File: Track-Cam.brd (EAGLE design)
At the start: 65 x 56 mm, 37 parts, among them IC1 STM32F042KT/M, IC2 BD6211F/M, IC3 BD6211F/M, X1 RASPI_BOARD_B+#_HC

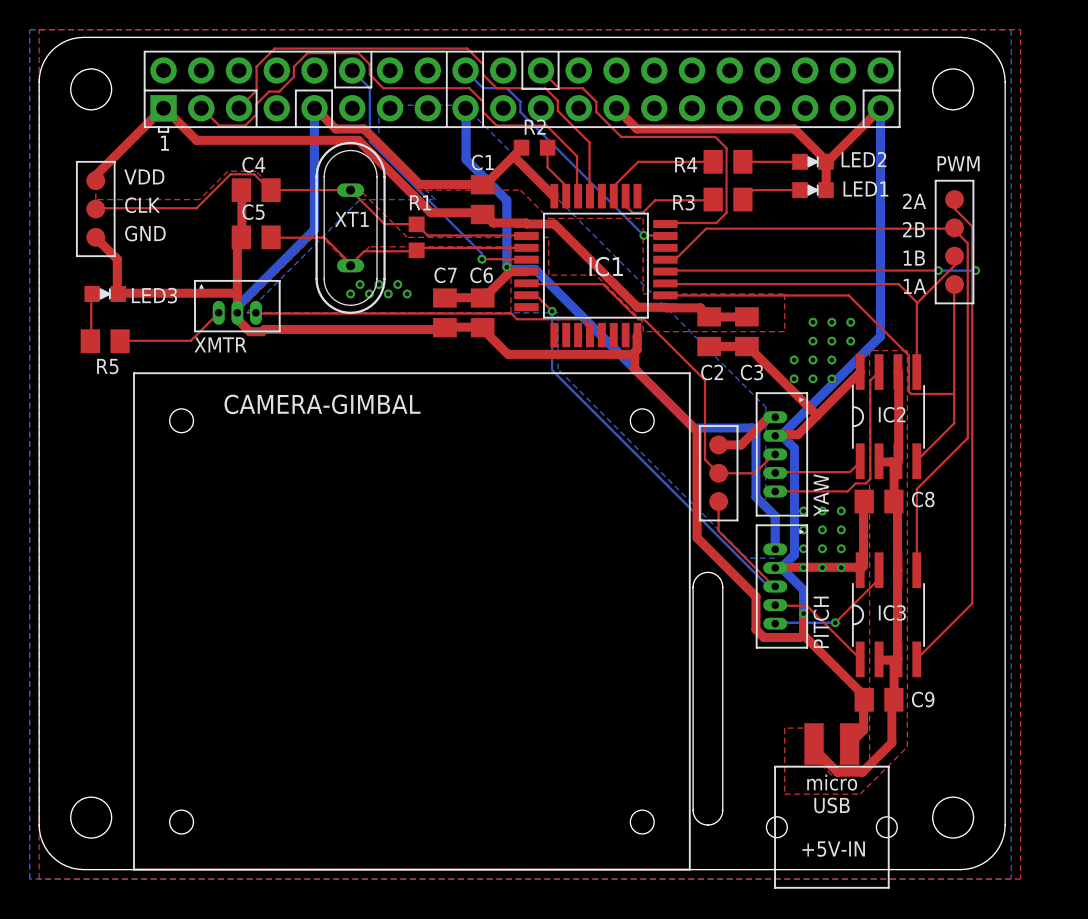
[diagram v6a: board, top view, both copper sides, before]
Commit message: improve silk design
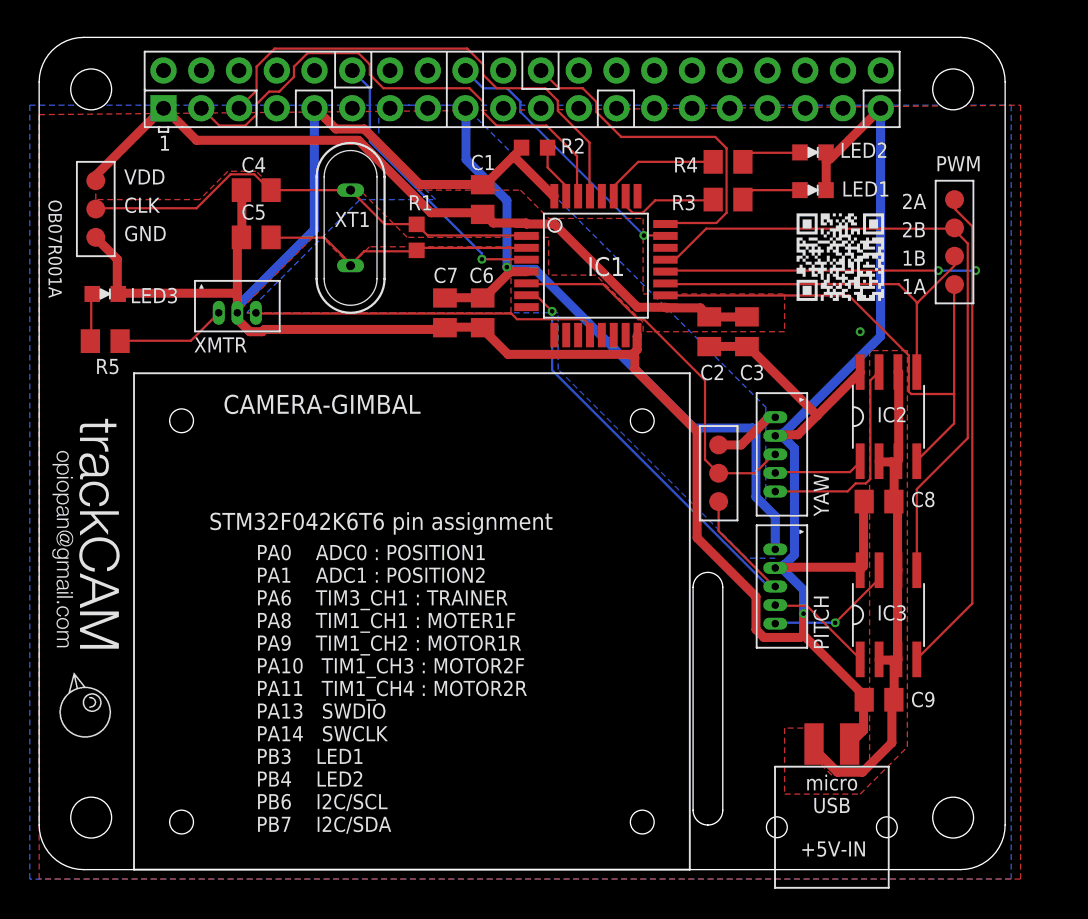
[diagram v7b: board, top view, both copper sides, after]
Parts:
- added U$1: PRODUCT-LOGO-TRACKCAM, logo:TRACKCAM-LOGO
- added U$2: OPIOPAN-LOGO, logo:OPIOPAN-LOGO
- added U$3: (no value), logo:TRACKCAM-QRCODE
- moved LED2 0.63 mm to (52.1, 48.3)
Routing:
- net GND: track 213.5 -> 198.2 mm, vias 25 -> 2
- net +3V3: vias 8 -> 1
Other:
- board text added: "OB07R001A"
- board text added: "PA0 ADC0 : POSITION1 PA1 ADC1 : POSITION2 PA6 TIM3_CH1 : TRAINER PA8 TIM1_CH1 : MOTER1F PA9 TIM1_CH2 : MOTOR1R PA10 TIM1_CH3 : MOTOR2F PA11 TIM1_CH4 : MOTOR2R PA13 SWDIO PA14 SWCLK PB3 LED1 PB4 LED2 PB6 I2C/SCL PB7 I2C/SDA"
- board text added: "STM32F042K6T6 pin assignment"
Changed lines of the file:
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@@
 <setting verticaltext="up"/>
 </settings>
-<grid distance="25" unitdist="mil" unit="mil" style="lines" multiple="1" display="no" altdistance="12.5" altunitdist="mil" altunit="mil"/>
+<grid distance="25" unitdist="mil" unit="mil" style="lines" multiple="1" display="yes" altdistance="8" altunitdist="mil" altunit="mil"/>
 <layers>
 <layer number="1" name="Top" color="4" fill="1" visible="yes" active="yes"/>
-<layer number="16" name="Bottom" color="1" fill="1" visible="no" active="yes"/>
+<layer number="16" name="Bottom" color="1" fill="1" visible="yes" active="yes"/>
 <layer number="17" name="Pads" color="2" fill="1" visible="yes" active="yes"/>
 <layer number="18" name="Vias" color="2" fill="1" visible="yes" active="yes"/>
@@
 <layer number="40" name="bKeepout" color="1" fill="11" visible="yes" active="yes"/>
 <layer number="41" name="tRestrict" color="4" fill="10" visible="yes" active="yes"/>
-<layer number="42" name="bRestrict" color="1" fill="10" visible="yes" active="yes"/>
+<layer number="42" name="bRestrict" color="1" fill="10" visible="no" active="yes"/>
 <layer number="43" name="vRestrict" color="2" fill="10" visible="yes" active="yes"/>
 <layer number="44" name="Drills" color="7" fill="1" visible="no" active="yes"/>
@@
 <wire x1="46.99" y1="23.495" x2="44.45" y2="23.495" width="0.127" layer="21"/>
 <wire x1="44.45" y1="23.495" x2="44.45" y2="29.845" width="0.127" layer="21"/>
+<polygon width="0" layer="41" spacing="1.778">
+<vertex x="14.9225" y="45.085"/>
+<vertex x="17.145" y="45.085"/>
+<vertex x="17.145" y="43.18"/>
+<vertex x="14.9225" y="43.18"/>
+</polygon>
+<wire x1="37.592" y1="49.9872" x2="37.592" y2="52.4256" width="0.127" layer="21"/>
+<wire x1="37.592" y1="52.4256" x2="40.0304" y2="52.4256" width="0.127" layer="21"/>
+<wire x1="40.0304" y1="52.4256" x2="40.0304" y2="49.9872" width="0.127" layer="21"/>
+<text x="0.635" y="45.085" size="0.889" layer="21" font="vector" rot="SR270">OB07R001A</text>
+<text x="14.605" y="2.54" size="1.016" layer="21" font="vector">PA0    ADC0 : POSITION1
+PA1    ADC1 : POSITION2
+PA6    TIM3_CH1 : TRAINER
+PA8    TIM1_CH1 : MOTER1F
+PA9    TIM1_CH2 : MOTOR1R
+PA10   TIM1_CH3 : MOTOR2F
+PA11   TIM1_CH4 : MOTOR2R
+PA13   SWDIO
+PA14   SWCLK
+PB3    LED1
+PB4    LED2
+PB6    I2C/SCL
+PB7    I2C/SDA</text>
+<text x="11.43" y="22.86" size="1.143" layer="21" font="vector">STM32F042K6T6 pin assignment</text>
 </plain>
 <attributes>
@@
 </element>
 <element name="R2" library="generic" package="SMD1608" value="10K" x="33.3375" y="48.5775" smashed="yes" rot="R180">
-<attribute name="NAME" x="32.55" y="49.4515" size="1.016" layer="25"/>
+<attribute name="NAME" x="35.09" y="48.1815" size="1.016" layer="25"/>
 <attribute name="VALUE" x="34.1375" y="50.2275" size="1.016" layer="27" rot="R180"/>
 </element>
@@
 <attribute name="VALUE" x="51.27" y="44.02" size="1.016" layer="27"/>
 </element>
-<element name="LED2" library="gen-discrete" package="LED1608" value="LED1608" x="52.07" y="47.625" smashed="yes">
-<attribute name="NAME" x="53.8735" y="47.259" size="1.016" layer="25" font="vector"/>
-<attribute name="VALUE" x="51.27" y="45.925" size="1.016" layer="27"/>
+<element name="LED2" library="gen-discrete" package="LED1608" value="LED1608" x="52.07" y="48.26" smashed="yes">
+<attribute name="NAME" x="53.8735" y="47.894" size="1.016" layer="25" font="vector"/>
+<attribute name="VALUE" x="51.27" y="46.56" size="1.016" layer="27"/>
 </element>
 <element name="R3" library="gen-discrete" package="SMD2012" value="330" x="46.355" y="45.085" smashed="yes">
@@
 <attribute name="VALUE" x="16.256" y="40.767" size="0.8128" layer="27" font="vector" rot="R180"/>
 </element>
+<element name="U$1" library="logo" package="TRACKCAM-LOGO" value="PRODUCT-LOGO-TRACKCAM" x="0.635" y="31.115" rot="R270"/>
+<element name="U$2" library="logo" package="OPIOPAN-LOGO" value="OPIOPAN-LOGO" x="0.8382" y="13.335" rot="R270"/>
+<element name="U$3" library="logo" package="TRACKCAM-QRCODE" value="" x="50.165" y="37.465"/>
 </elements>
 <signals>
@@
 <vertex x="22.86" y="51.435"/>
 </polygon>
-<via x="20.955" y="38.735" extent="1-16" drill="0.3048"/>
-<via x="21.59" y="39.37" extent="1-16" drill="0.3048"/>
-<via x="22.225" y="38.735" extent="1-16" drill="0.3048"/>
-<via x="22.86" y="39.37" extent="1-16" drill="0.3048"/>
-<via x="23.495" y="38.735" extent="1-16" drill="0.3048"/>
-<via x="24.13" y="39.37" extent="1-16" drill="0.3048"/>
-<via x="24.765" y="38.735" extent="1-16" drill="0.3048"/>
 </signal>
 <signal name="BOOT0">
@@
 <contactref element="R4" pad="2"/>
 <contactref element="LED2" pad="A"/>
-<wire x1="47.355" y1="47.625" x2="51.195" y2="47.625" width="0.1524" layer="1"/>
+<wire x1="48.006" y1="48.2346" x2="51.1302" y2="48.2346" width="0.1524" layer="1"/>
+<wire x1="47.3964" y1="47.625" x2="48.006" y2="48.2346" width="0.1524" layer="1"/>
+<wire x1="47.3964" y1="47.625" x2="47.355" y2="47.625" width="0.1524" layer="1"/>
+<wire x1="51.1302" y1="48.2346" x2="51.195" y2="48.26" width="0.1524" layer="1"/>
 </signal>
 <signal name="5V0B">
@@
 <wire x1="52.959" y1="47.625" x2="52.959" y2="45.72" width="0.6096" layer="1"/>
 <wire x1="52.959" y1="45.72" x2="52.945" y2="45.72" width="0.6096" layer="1"/>
-<wire x1="52.959" y1="47.625" x2="52.945" y2="47.625" width="0.6096" layer="1"/>
+<wire x1="52.959" y1="47.625" x2="52.945" y2="48.26" width="0.6096" layer="1"/>
 <wire x1="56.6166" y1="51.2064" x2="53.1876" y2="47.7774" width="0.6096" layer="1"/>
-<wire x1="53.1876" y1="47.7774" x2="52.945" y2="47.625" width="0.6096" layer="1"/>
 <wire x1="56.6166" y1="51.2064" x2="56.63" y2="51.23" width="0.6096" layer="1"/>
-<wire x1="50.8254" y1="49.8348" x2="52.8066" y2="47.8536" width="0.6096" layer="1"/>
-<wire x1="40.2336" y1="49.8348" x2="50.8254" y2="49.8348" width="0.6096" layer="1"/>
-<wire x1="38.862" y1="51.2064" x2="40.2336" y2="49.8348" width="0.6096" layer="1"/>
-<wire x1="52.8066" y1="47.8536" x2="52.945" y2="47.625" width="0.6096" layer="1"/>
-<wire x1="38.862" y1="51.2064" x2="38.85" y2="51.23" width="0.6096" layer="1"/>
 <wire x1="25.6032" y1="46.101" x2="29.7942" y2="46.101" width="0.6096" layer="1"/>
 <wire x1="21.8694" y1="49.8348" x2="25.6032" y2="46.101" width="0.6096" layer="1"/>
@@
 <wire x1="34.5948" y1="45.339" x2="34.665" y2="45.315" width="0.6096" layer="1"/>
 <polygon width="0.6096" layer="1" spacing="1.778" isolate="0.3048" thermals="no" rank="6">
-<vertex x="0" y="56.515"/>
-<vertex x="66.04" y="56.515"/>
+<vertex x="0" y="50.8"/>
+<vertex x="66.04" y="51.435"/>
 <vertex x="66.04" y="-0.635"/>
 <vertex x="0" y="-0.635"/>
 </polygon>
 <polygon width="0.6096" layer="16" spacing="1.778" isolate="0.3048" thermals="no" rank="6">
-<vertex x="-0.635" y="56.515"/>
-<vertex x="65.405" y="56.515"/>
+<vertex x="-0.635" y="51.435"/>
+<vertex x="65.405" y="51.435"/>
 <vertex x="65.405" y="-0.635"/>
 <vertex x="-0.635" y="-0.635"/>
 </polygon>
-<via x="52.07" y="36.83" extent="1-16" drill="0.3048"/>
-<via x="53.34" y="36.83" extent="1-16" drill="0.3048"/>
-<via x="54.61" y="36.83" extent="1-16" drill="0.3048"/>
-<via x="54.61" y="35.56" extent="1-16" drill="0.3048"/>
-<via x="53.34" y="35.56" extent="1-16" drill="0.3048"/>
-<via x="52.07" y="35.56" extent="1-16" drill="0.3048"/>
-<via x="50.8" y="34.29" extent="1-16" drill="0.3048"/>
-<via x="52.07" y="34.29" extent="1-16" drill="0.3048"/>
-<via x="53.34" y="34.29" extent="1-16" drill="0.3048"/>
-<via x="53.34" y="33.02" extent="1-16" drill="0.3048"/>
-<via x="52.07" y="33.02" extent="1-16" drill="0.3048"/>
-<via x="50.8" y="33.02" extent="1-16" drill="0.3048"/>
-<via x="51.435" y="24.13" extent="1-16" drill="0.3048"/>
-<via x="52.705" y="24.13" extent="1-16" drill="0.3048"/>
-<via x="53.975" y="24.13" extent="1-16" drill="0.3048"/>
-<via x="53.975" y="22.86" extent="1-16" drill="0.3048"/>
-<via x="52.705" y="22.86" extent="1-16" drill="0.3048"/>
-<via x="51.435" y="22.86" extent="1-16" drill="0.3048"/>
-<via x="51.435" y="21.59" extent="1-16" drill="0.3048"/>
-<via x="52.705" y="21.59" extent="1-16" drill="0.3048"/>
-<via x="53.975" y="21.59" extent="1-16" drill="0.3048"/>
-<via x="53.975" y="20.32" extent="1-16" drill="0.3048"/>
-<via x="52.705" y="20.32" extent="1-16" drill="0.3048"/>
-<via x="51.435" y="20.32" extent="1-16" drill="0.3048"/>
+<via x="55.245" y="36.195" extent="1-16" drill="0.3048"/>
 </signal>
 <signal name="MOTOR2_POS">
